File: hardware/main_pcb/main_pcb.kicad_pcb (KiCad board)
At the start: 4 copper layers, 60 x 70 mm, 64 parts, among them J1 Boot, J2 Debug, J3 USB4110, J4 MEM2085, J5 CUI_SJ_3523, Q1 AM2336N, SW1 CS1102, SW2 CS1102, SW3 CS1102, SW4 CS1102, SW5 CK-JS102011SAQN, SW6 COM09426, U1 BQ21040, U2 STM32H533CET, U3 MCP1824, U4 IS67WVS4M8BLL-104NLA1, U5 MCP6009, U6 WF0200BTYAJDNN0, X1 ASE-16.000MHZ, Y1 CM315D32768HZFT

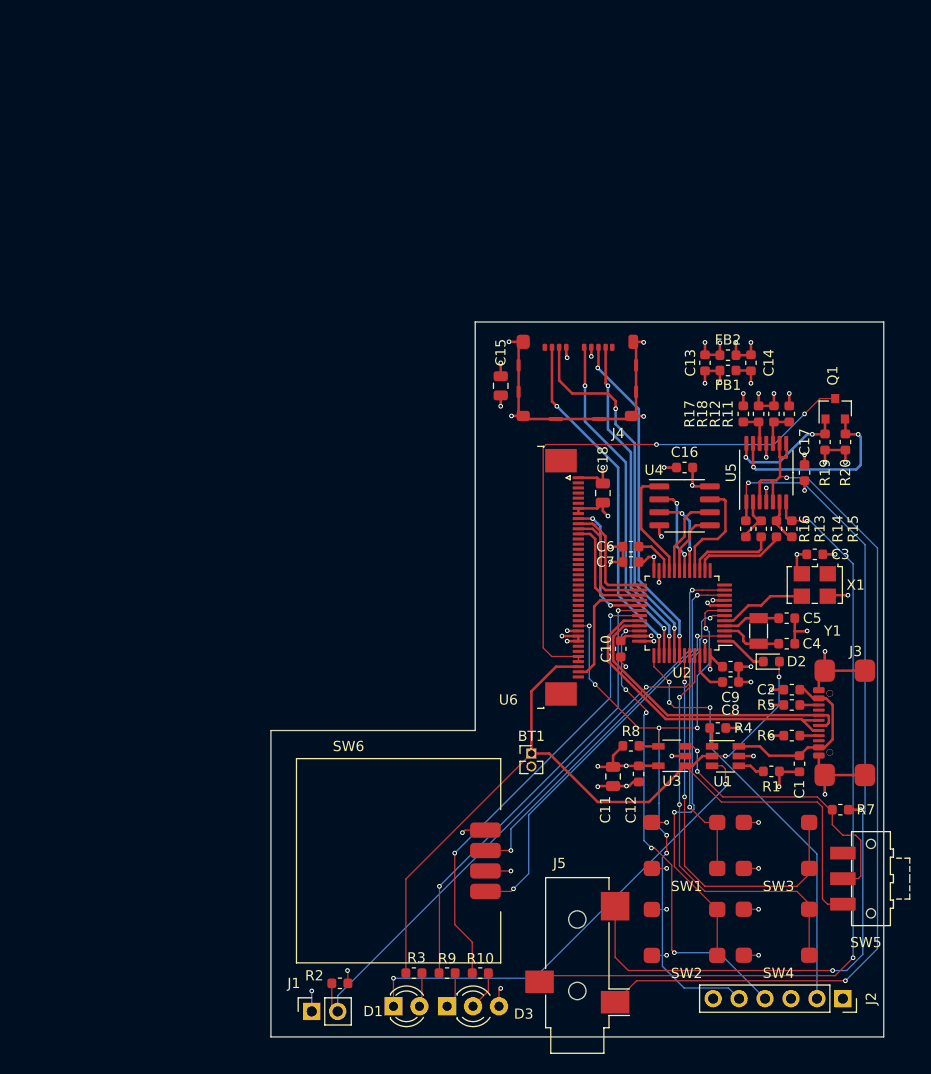
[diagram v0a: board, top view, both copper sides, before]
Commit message: Layout for new PCB geometry.
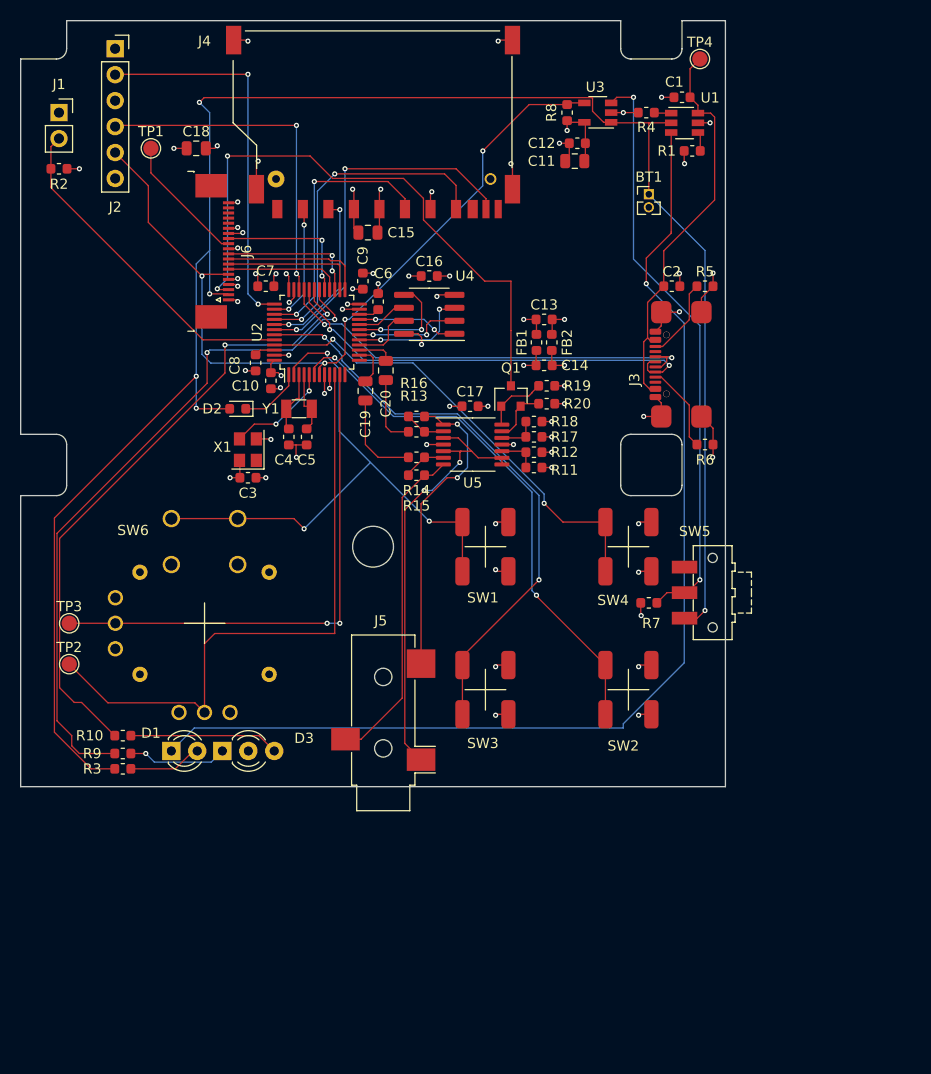
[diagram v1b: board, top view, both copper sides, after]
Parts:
- removed U6: WF0200BTYAJDNN0, Connector_FFC-FPC:TE_4-1734839-0_1x40-1MP_P0.5mm_Horizontal
- added C19: 10u, Capacitor_SMD:C_0805_2012Metric, F.Cu at (84.2, 86.8)
- added C20: 10u, Capacitor_SMD:C_0805_2012Metric, F.Cu at (86.2, 84.8)
- added J6: SFV20R-2ST, main_pcb:FPC_1x20_P0.5mm_top, F.Cu at (69.5, 80.5)
- added TP1: TestPoint_Small, TestPoint:TestPoint_Pad_D1.5mm, F.Cu at (63.2, 63.0)
- added TP2: TestPoint_Small, TestPoint:TestPoint_Pad_D1.5mm, F.Cu at (55.2, 113.5)
- added TP3: TestPoint_Small, TestPoint:TestPoint_Pad_D1.5mm, F.Cu at (55.2, 109.5)
- added TP4: TestPoint_Small, TestPoint:TestPoint_Pad_D1.5mm, F.Cu at (117.0, 54.2)
- D1: value LED -> 151031SS06000
- D3: value LED_Dual_AAC -> LTL-1BEHJ
- J4: value MEM2085 -> SD-4-B; footprint main_pcb:MEM2085 -> main_pcb:SD-4-B
- J5: value CUI_SJ_3523 -> STX-3500-3NTR
- Q1: value AM2336N -> SSM3K376R
- SW1, SW2, SW3, SW4: value CS1102 -> LL3301BF065QJ; footprint main_pcb:CS1102 -> main_pcb:LL3301-J
- SW6: value COM09426 -> THB001P; footprint main_pcb:COM09426 -> main_pcb:THB001P
- U2: value STM32H533CET -> STM32H523CET
- U3: value MCP1824 -> MCP1824T-3302E/OT
- U5: value MCP6009 -> MCP6009T-E/ST
- X1: footprint Oscillator:Oscillator_SMD_SeikoEpson_SG8002LB-4Pin_5.0x3.2mm -> Oscillator:Oscillator_SMD_Abracon_ASE-4Pin_3.2x2.5mm
- moved J2 117.2 mm to (59.8, 53.2), turned to 0 degrees
- moved J1 91.4 mm to (54.2, 59.5), turned to 0 degrees
- moved R2 84.4 mm to (54.2, 65.0)
- moved C1 66.3 mm to (115.2, 58.0), turned to 180 degrees
- moved U3 63.4 mm to (107.0, 59.5)
- moved R8 62.3 mm to (104.0, 59.5), turned to 90 degrees
- moved U1 62.1 mm to (115.5, 60.5)
- moved C12 62.0 mm to (105.0, 62.5), turned to 180 degrees
- moved R1 61.2 mm to (116.2, 63.2), turned to 180 degrees
- moved R4 60.7 mm to (111.8, 59.5), turned to 180 degrees
- moved C11 60.4 mm to (104.8, 64.2), turned to 180 degrees
- moved D2 57.8 mm to (71.8, 88.5), turned to 180 degrees
- moved X1 57.1 mm to (72.8, 92.5), turned to 90 degrees
- moved C8 56.0 mm to (73.5, 84.0), turned to 270 degrees
- moved C3 56.0 mm to (72.8, 95.2), turned to 0 degrees
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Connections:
- D3 pad 2: Net-(D3-Pad2) -> GND
- D3 pad 3: GND -> Net-(D3-Pad3)
- J4 pad 3: Net-(J4-Pad3) -> GND
- R10 pad 2: Net-(D3-Pad2) -> Net-(D3-Pad3)
- R13 pad 1: Net-(R13-Pad1) -> Net-(C20-Pad2)
- R14 pad 1: Net-(R14-Pad1) -> Net-(C19-Pad2)
- SW1 pad 2: Net-(SW1-Pad2) -> +3V3
- SW1 pad 3: +3V3 -> Net-(SW1-Pad3)
- SW1 pad 4: Net-(SW1-Pad2) -> Net-(SW1-Pad3)
- SW2 pad 2: Net-(SW2-Pad2) -> +3V3
- SW2 pad 3: +3V3 -> Net-(SW2-Pad3)
- SW2 pad 4: Net-(SW2-Pad2) -> Net-(SW2-Pad3)
- SW3 pad 2: Net-(SW3-Pad2) -> +3V3
- SW3 pad 3: +3V3 -> Net-(SW3-Pad3)
- SW3 pad 4: Net-(SW3-Pad2) -> Net-(SW3-Pad3)
- SW4 pad 2: Net-(SW4-Pad2) -> +3V3
- SW4 pad 3: +3V3 -> Net-(SW4-Pad3)
- SW4 pad 4: Net-(SW4-Pad2) -> Net-(SW4-Pad3)
- U2 pad 10: Net-(SW6-Pad1) -> Net-(SW6-PadX2)
- U2 pad 11: Net-(SW6-Pad3) -> Net-(SW6-PadY2)
- U2 pad 14: Net-(R14-Pad1) -> Net-(C19-Pad1)
- U2 pad 15: Net-(R13-Pad1) -> Net-(C20-Pad1)
- U2 pad 2: Net-(SW1-Pad2) -> Net-(SW1-Pad3)
- U2 pad 38: Net-(J4-Pad2) -> Net-(J4-Pad1)
- U2 pad 41: Net-(J4-Pad3) -> Net-(J4-Pad2)
- U2 pad 42: Net-(J4-PadCD) -> Net-(J4-Pad10)
- U2 pad 43: Net-(SW3-Pad2) -> Net-(SW3-Pad3)
- U2 pad 45: Net-(SW4-Pad2) -> Net-(SW4-Pad3)
- U2 pad 6: Net-(SW2-Pad2) -> Net-(SW2-Pad3)
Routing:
- net +BATT: track 99.1 -> 188.8 mm, vias 2 -> 5
- net Net-(D1-Pad1): track 46.2 -> 108.5 mm, vias 2 -> 1
- net Net-(SW6-PadX2): track 0.00 -> 60.4 mm
- net Net-(J5-PadT): track 88.5 -> 29.9 mm
- net Net-(SW3-Pad3): track 0.00 -> 57.3 mm, vias 0 -> 2
- net Net-(SW1-Pad3): track 0.00 -> 55.9 mm, vias 0 -> 3
- net Net-(SW2-Pad3): track 0.00 -> 52.6 mm, vias 0 -> 2
- net Net-(SW6-PadY2): track 0.00 -> 50.8 mm, vias 0 -> 2
- net Net-(J5-PadR): track 80.0 -> 32.2 mm, vias 2 -> 0
- net Net-(J5-PadS): track 91.2 -> 43.5 mm
- net Net-(SW4-Pad3): track 0.00 -> 45.4 mm, vias 0 -> 2
- net Net-(SW6-Pad1): track 41.7 -> 0.00 mm, vias 2 -> 0
- net Net-(SW4-Pad2): track 40.5 -> 0.00 mm, vias 2 -> 0
- net Net-(SW3-Pad2): track 39.2 -> 0.00 mm, vias 2 -> 0
- net Net-(SW2-Pad2): track 39.1 -> 0.00 mm, vias 2 -> 0
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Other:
- board size 60 x 70 mm -> 69 x 75 mm
- net class Default: via_dia 0.4572 -> 0.508
- rule via_min_size: 0.4 -> 0.508

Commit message: Joystick orientation, some trace cleanup, add text to PCB silkscreen.
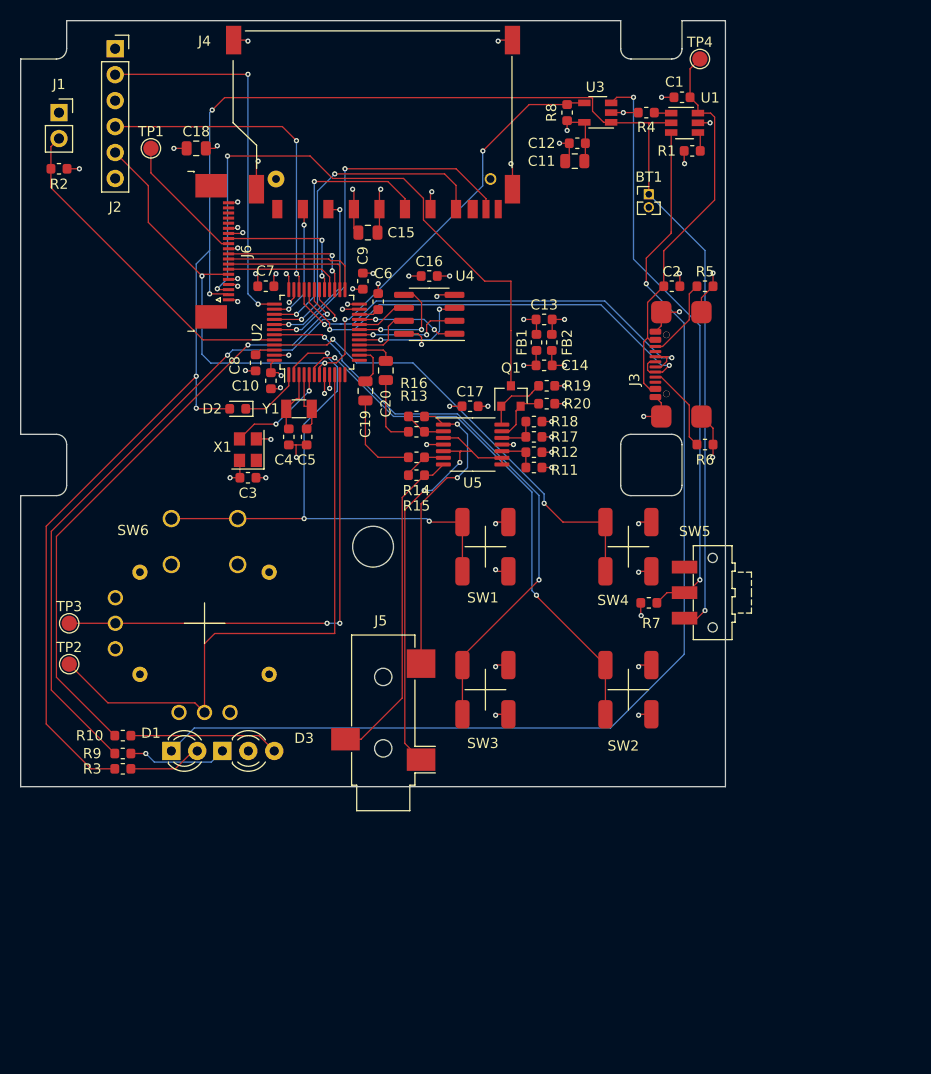
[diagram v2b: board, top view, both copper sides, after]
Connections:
- SW6 pad X1: +3V3 -> GND
- SW6 pad X3: GND -> +3V3
- SW6 pad Y1: GND -> +3V3
- SW6 pad Y3: +3V3 -> GND
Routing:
- net Net-(R9-Pad1): track 67.1 -> 64.2 mm
- net Net-(J3-PadA7): track 43.4 -> 45.8 mm
- net Net-(J3-PadA6): track 44.1 -> 46.1 mm
- net Net-(R10-Pad1): track 61.8 -> 60.3 mm
- net +BATT: track 188.8 -> 187.5 mm
- net Net-(J2-Pad4): track 34.0 -> 33.0 mm
- net Net-(D1-Pad1): track 108.5 -> 107.8 mm
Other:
- board text added: "GameSquirrel Rev 0.1 Copyright 2025 Jeff Lassahn Open Source Hardware License: CERN-OHL-P-2.0 https://github.com/jlassahn/gamesquirrel"
